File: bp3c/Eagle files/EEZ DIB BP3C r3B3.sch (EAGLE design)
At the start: 62 parts, among them IC1 TCA9534PWR, K1 RT424005, K2 RT424005, K3 RT424005, K4 RT424005, Q1 2N7002, Q2 2N7002, Q3 2N7002, Q4 2N7002, X1 ZL202-20G, X2 ZL202-20G, X3 ZL202-20G, X4 DS1023-2*14S21, X5 DS1022-2*20RF11, X6 DS1023-2*14S21, X7 N.C., X8 DS1023-2*14S21

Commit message: DIB v1.1, BP3C r3B3
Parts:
- removed X7: N.C., con-samtec:SSW-108-02-S-S
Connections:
- new net SPI4_CSC: X5-30.1
- new net SPI5_CSC: X5-34.1
- net +3V3: no longer X7-2.1, X7-3.1, X7-6.1
- net GND: no longer X5-30.1, X5-34.1, X7-1.1
- net I2C1_SCL: no longer X7-8.1
- net I2C1_SDA: no longer X7-7.1
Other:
- note added: "18 SPI3_MISO"
- note added: "20 SPI3_MOSI"
- note added: "22 SPI2_CSA"
- note added: "24 SPI2_MISO"
- note added: "26 SPI2_MOSI"
- note added: "28 SPI1_CSA"
- note added: "30 SPI2_CSC"
- note added: "32 SPI1_SCLK"
- note added: "34 SPI3_CSC"
- note added: "40-pin DIB v1.1 backplane socket"
- note added: "SPI1_CSB 27"
- note added: "SPI1_IRQ 25"
- note added: "SPI1_MISO 31"
- note added: "SPI1_MOSI 33"
- note added: "SPI2_CSB 21"
- note added: "SPI2_IRQ 19"
- note added: "SPI2_SCLK 23"
- note added: "SPI3_CSA 11"
- note added: "SPI3_CSB 13"
- note added: "SPI3_IRQ 9"
- note added: "SPI3_SCLK 17"
- note removed: "18 SPI5_MISO"
- note removed: "20 SPI5_MOSI"
- note removed: "22 SPI4_CSA"
- note removed: "24 SPI4_MISO"
- note removed: "26 SPI4_MOSI"
- note removed: "28 SPI2_CSA"
- note removed: "30 Gnd"
- note removed: "32 SPI2_SCLK"
- note removed: "34 Gnd"
- note removed: "40-pin MCU socket"
- note removed: "ADxL345 module connector (optional)"
- note removed: "SPI2_CSB 27"
- note removed: "SPI2_IRQ 25"
- note removed: "SPI2_MISO 31"
- note removed: "SPI2_MOSI 33"
- note removed: "SPI4_CSB 21"
- note removed: "SPI4_IRQ 19"
- note removed: "SPI4_SCLK 23"
- note removed: "SPI5_CSA 11"
- note removed: "SPI5_CSB 13"
- note removed: "SPI5_IRQ 9"
- note removed: "SPI5_SCLK 17"

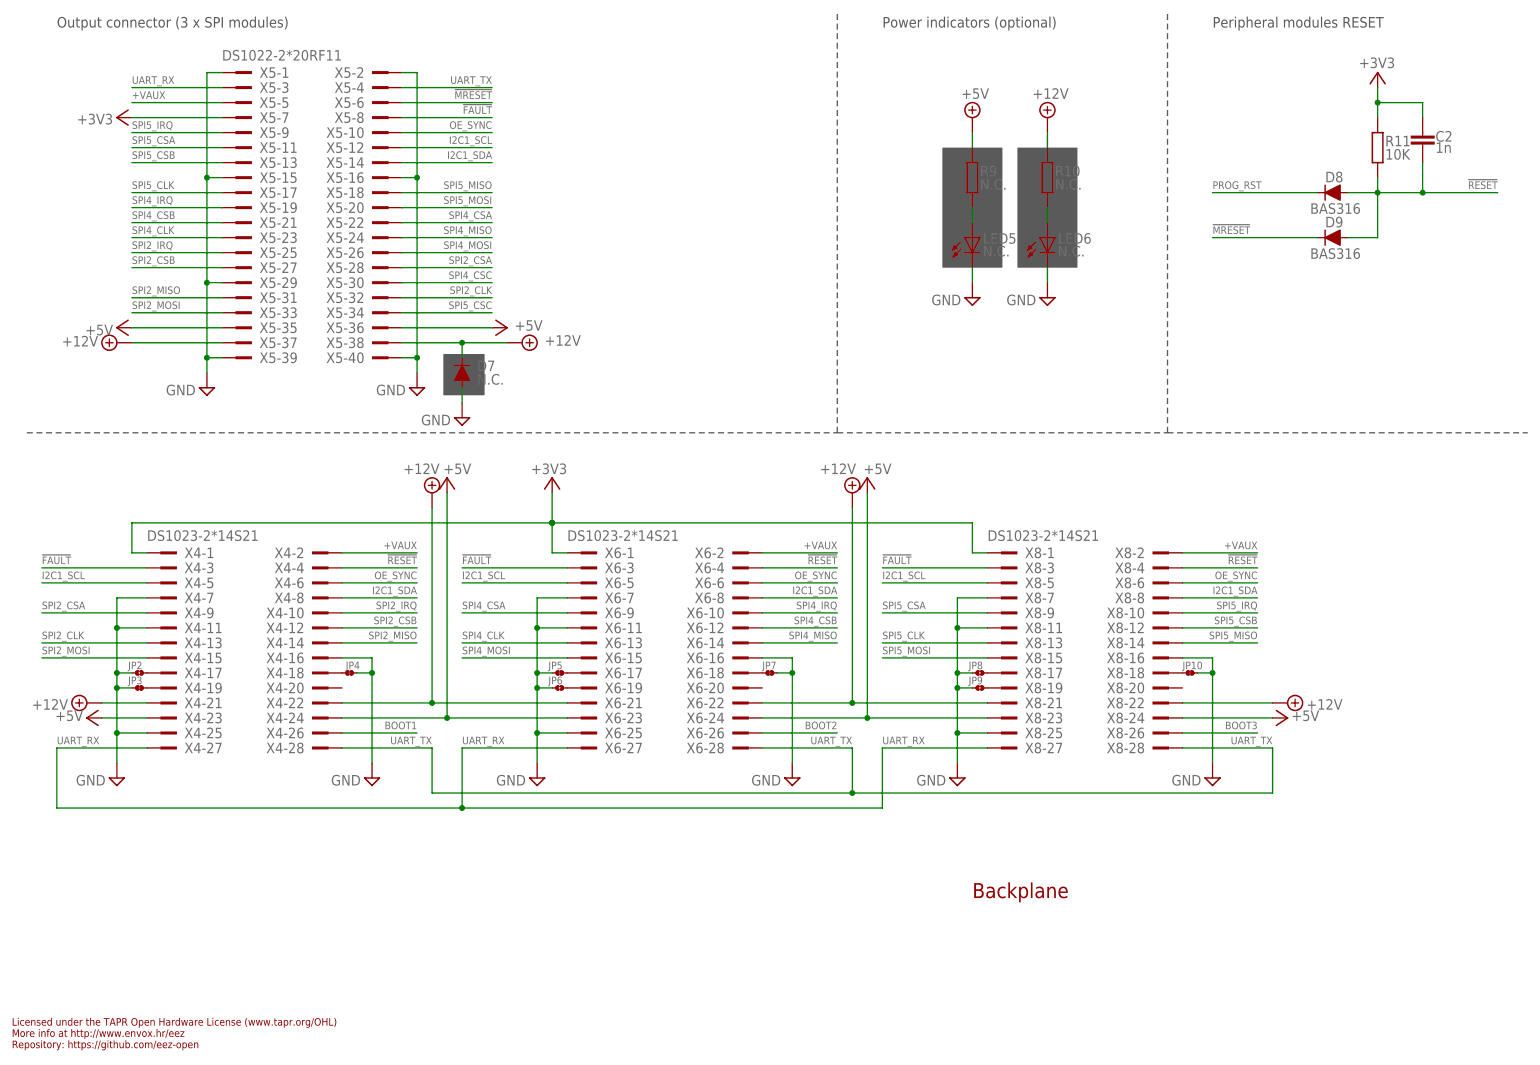
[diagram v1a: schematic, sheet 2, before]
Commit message: BP3C new ZD1-ZD4 type
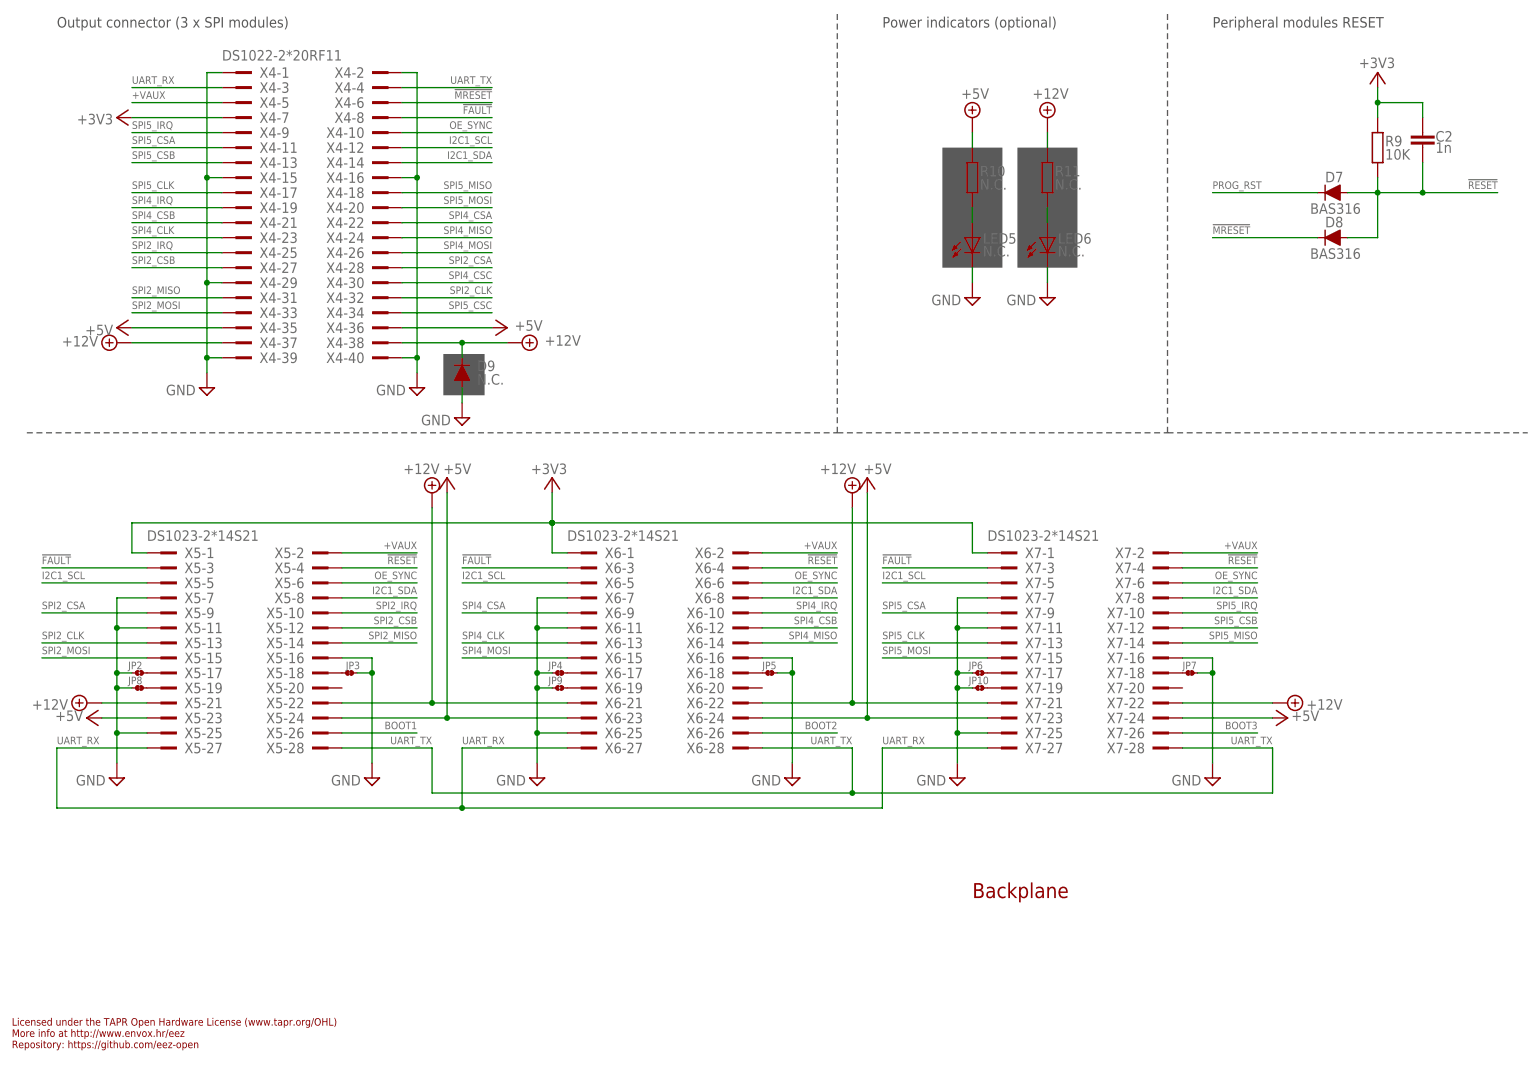
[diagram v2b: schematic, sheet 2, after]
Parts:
- D1, D2: value N.C. -> BAS316
- D3, D4: value BAS316 -> N.C.
- D7: value N.C. -> BAS316; device MyLib6:DIODEDO214AA -> EEZ_Lib1:DIODESOD323R
- D9: value BAS316 -> N.C.; device EEZ_Lib1:DIODESOD323R -> MyLib6:DIODEDO214AA
- JP10: value JP2-NOCUT -> JP2-CUT; device EEZ_Lib1:JP2-NOCUT -> EEZ_Lib1:JP2-CUT
- JP8: value JP2-CUT -> JP2-NOCUT; device EEZ_Lib1:JP2-CUT -> EEZ_Lib1:JP2-NOCUT
- R1, R5: value 100K -> N.C.
- R11: value 10K -> N.C.
- R6, R8: value N.C. -> 100K
- R9: value N.C. -> 10K
- X4: value DS1023-2*14S21 -> DS1022-2*20RF11; device EEZ_connectors:TSW-114-07-F-D -> EEZ_connectors:ZL212-40KG
- X5: value DS1022-2*20RF11 -> DS1023-2*14S21; device EEZ_connectors:ZL212-40KG -> EEZ_connectors:TSW-114-07-F-D
- ZD1, ZD2, ZD3, ZD4: value SMAJ18A -> MM3Z18VT1G; device EEZ_Lib1:PSMAXX -> EEZ_Lib1:ZENER-DIODESOD323R
- renumbered OSHWA to LABEL1, X8 to X7
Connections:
- removed net N$104 (its old number): D4.A, ZD2.A
- new net N$128: D2.A, ZD2.A
- net !FAULT: now also X4-8.1, X5-3.1; no longer X4-3.1, X5-8.1
- net !MRESET: now also D8.C, X4-6.1; no longer D9.C, X5-6.1
- net !RESET: now also D7.A, R9.2, X5-4.1; no longer D9.A, R11.2, X4-4.1
- net +12V: now also D9.C, R11.1, X4-37.1, X4-38.1, X5-21.1, X5-22.1; no longer D7.C, R10.1, X4-21.1, X4-22.1, X5-37.1, X5-38.1
- net +3V3: now also R9.1, X4-7.1, X5-1.1; no longer R11.1, X4-1.1, X5-7.1
- net +5V: now also D1.C, D2.C, R10.1, X4-35.1, X4-36.1, X5-23.1, X5-24.1; no longer D3.C, D4.C, R9.1, X4-23.1, X4-24.1, X5-35.1, X5-36.1
- net +VAUX: now also X4-5.1, X5-2.1; no longer X4-2.1, X5-5.1
- net BOOT1: now also X5-26.1; no longer X4-26.1
- net CH1_IN+: now also K4-1.P; no longer K1-1.P
- net CH1_OUT+: now also K3-1.O, K4-1.S, K4-2.O; no longer K1-1.S, K1-2.O, K2-1.O
- net CH1_OUT-: now also K1-1.O, K2-1.O, K3-2.O; no longer K2-2.O, K3-1.O, K4-1.O
- net CH2_IN+: now also K4-2.P; no longer K1-2.P
- net CH2_IN-: now also K3-2.P, K4-1.O; no longer K1-1.O, K2-2.P
- net CH2_OUT+: now also K2-1.P, K3-1.S; no longer K2-1.S, K4-1.P
- net CH2_OUT-: now also K1-1.P, K1-2.P, K3-2.S; no longer K2-2.S, K3-1.P, K3-2.P
- net CH3-: now also K1-2.O; no longer K3-2.O
- net GND: now also D9.A, JP10.1, JP3.2, JP4.1, JP5.2, R6.1, R8.1, X4-1.1, X4-15.1, X4-2.1, X4-29.1, X4-39.1, X4-40.1, X5-11.1, X5-25.1, X5-7.1; no longer D7.A, JP10.2, JP3.1, JP4.2, JP5.1, R1.1, R5.1, X4-11.1, X4-25.1, X4-7.1, X5-1.1, X5-15.1, X5-2.1, X5-29.1, X5-39.1, X5-40.1
- net I2C1_SCL: now also X4-12.1, X5-5.1; no longer X4-5.1, X5-12.1
- net I2C1_SDA: now also X4-14.1, X5-8.1; no longer X4-8.1, X5-14.1
- net N$10: now also JP4.2; no longer JP5.2
- net N$101: now also K4K.C2, Q3.D, R5.2, ZD3.C; no longer K1K.C2, Q2.D, R6.2, ZD2.C
- net N$102: now also K3K.C2, Q2.D, R3.2, ZD2.C; no longer K2K.C2, Q3.D, R7.2, ZD3.C
- net N$11: now also JP9.2; no longer JP6.2
- net N$12: now also JP7.1; no longer JP10.1
- net N$13: now also JP6.2; no longer JP8.2
- net N$14: now also JP10.2; no longer JP9.2
- net N$17: now also K1K.C2, R1.2; no longer K3K.C2, R3.2
- net N$18: now also D1.A; no longer D3.A
- net N$19: now also R1.1; no longer R3.1
- net N$2: now also JP3.1, X5-18.1; no longer JP4.1, X4-18.1
- net N$20: now also K2K.C2, R7.2; no longer K4K.C2, R8.2
- net N$22: now also R7.1; no longer R8.1
- net N$3: now also R10.2; no longer R9.2
- net N$4: now also R11.2; no longer R10.2
- net N$5: now also X5-17.1; no longer X4-17.1
- net N$6: now also JP8.2, X5-19.1; no longer JP3.2, X4-19.1
- net N$7: now also LED3.C, R5.1; no longer LED2.C, R6.1
- net N$8: now also LED2.C, R3.1; no longer LED3.C, R7.1
- net N$9: now also JP5.1; no longer JP7.1
- net OE_SYNC: now also X4-10.1, X5-6.1; no longer X4-6.1, X5-10.1
- net OUT_CGND: now also D3.C, R2.2; no longer D1.C, R1.2
- net OUT_PAR: now also D4.A, Q2.G; no longer D2.A, Q3.G
- net OUT_SER: now also D3.A, D4.C, Q3.G, R6.2; no longer D1.A, D2.C, Q2.G, R2.2
- net OUT_SRA: now also R8.2; no longer R5.2
- net PROG_RST: now also D7.C; no longer D8.C
- net SER_PAR: now also K3-1.P, K4-2.S; no longer K1-2.S, K2-1.P
- net SPI2_CLK: now also X4-32.1, X5-13.1; no longer X4-13.1, X5-32.1
- net SPI2_CSA: now also X4-28.1, X5-9.1; no longer X4-9.1, X5-28.1
- net SPI2_CSB: now also X4-27.1, X5-12.1; no longer X4-12.1, X5-27.1
- net SPI2_IRQ: now also X4-25.1, X5-10.1; no longer X4-10.1, X5-25.1
- net SPI2_MISO: now also X4-31.1, X5-14.1; no longer X4-14.1, X5-31.1
- net SPI2_MOSI: now also X4-33.1, X5-15.1; no longer X4-15.1, X5-33.1
- net SPI4_CLK: now also X4-23.1; no longer X5-23.1
- net SPI4_CSA: now also X4-22.1; no longer X5-22.1
- net SPI4_CSB: now also X4-21.1; no longer X5-21.1
- net SPI4_CSC: now also X4-30.1; no longer X5-30.1
- net SPI4_IRQ: now also X4-19.1; no longer X5-19.1
- net SPI4_MISO: now also X4-24.1; no longer X5-24.1
- net SPI4_MOSI: now also X4-26.1; no longer X5-26.1
- net SPI5_CLK: now also X4-17.1; no longer X5-17.1
- net SPI5_CSA: now also X4-11.1; no longer X5-11.1
- net SPI5_CSB: now also X4-13.1; no longer X5-13.1
- net SPI5_CSC: now also X4-34.1; no longer X5-34.1
- net SPI5_IRQ: now also X4-9.1; no longer X5-9.1
- net SPI5_MISO: now also X4-18.1; no longer X5-18.1
- net SPI5_MOSI: now also X4-20.1; no longer X5-20.1
- net UART_RX: now also X4-3.1, X5-27.1; no longer X4-27.1, X5-3.1
- net UART_TX: now also X4-4.1, X5-28.1; no longer X4-28.1, X5-4.1
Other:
- moved on the sheet: D1, D2, D3, D4, D5, D7, D8, D9, JP3, JP4, JP5, JP6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

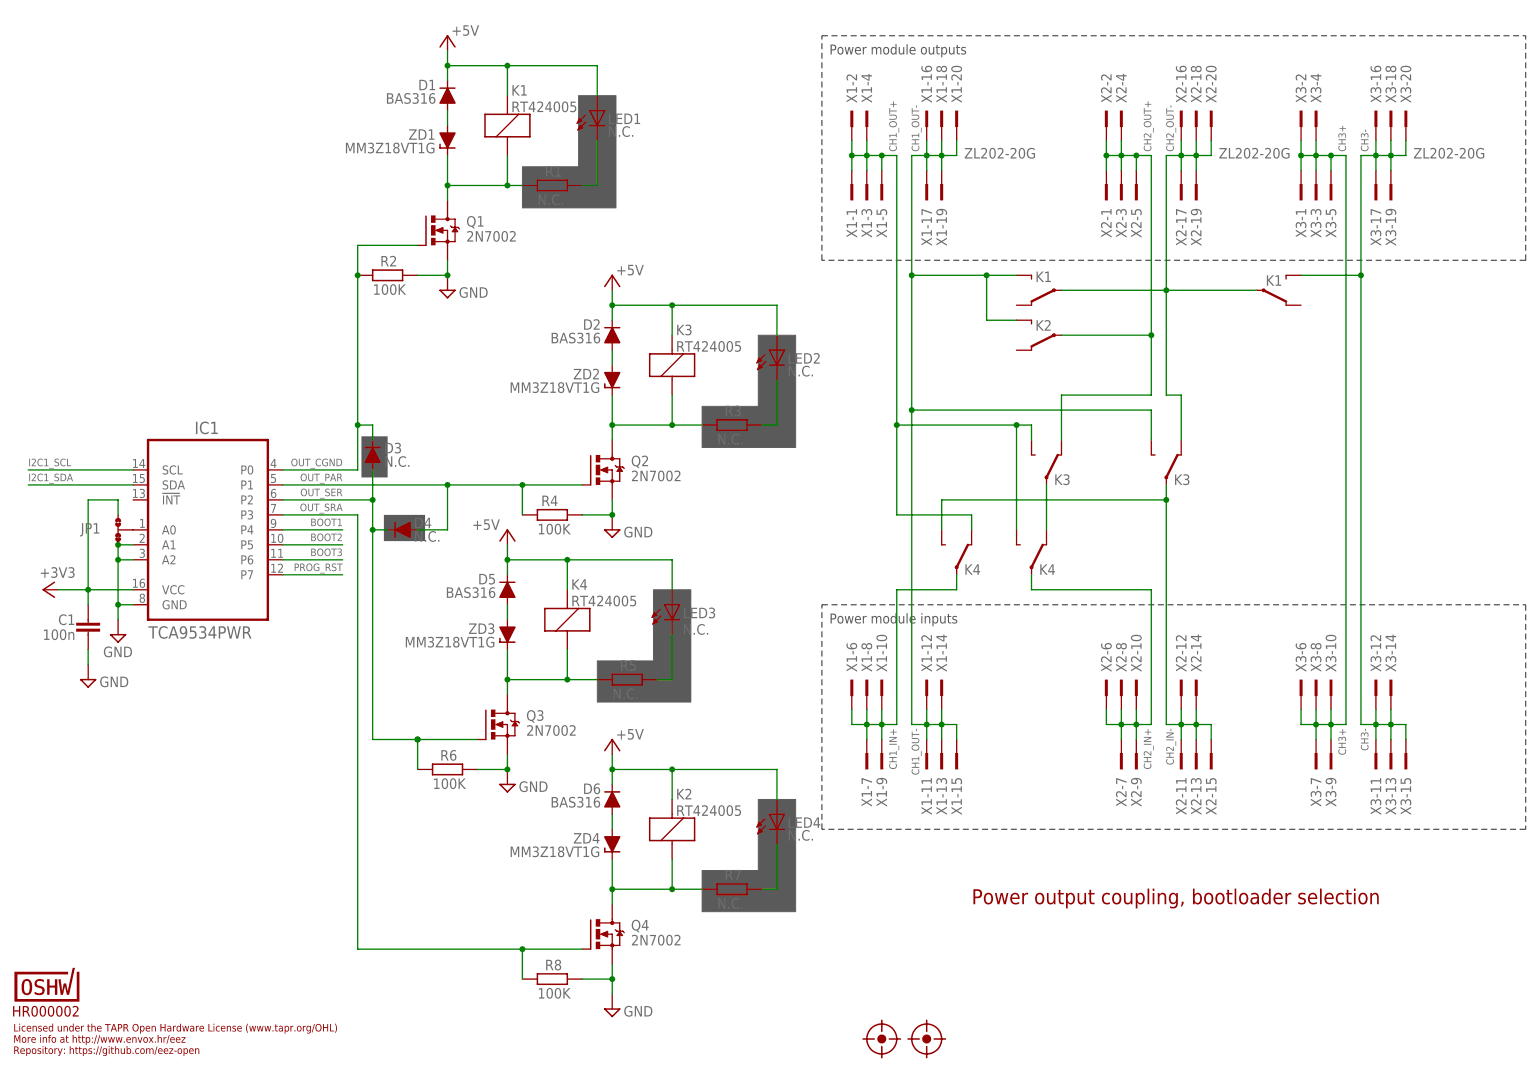
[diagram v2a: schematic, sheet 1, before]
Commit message: BP3C bottom layer cleanup
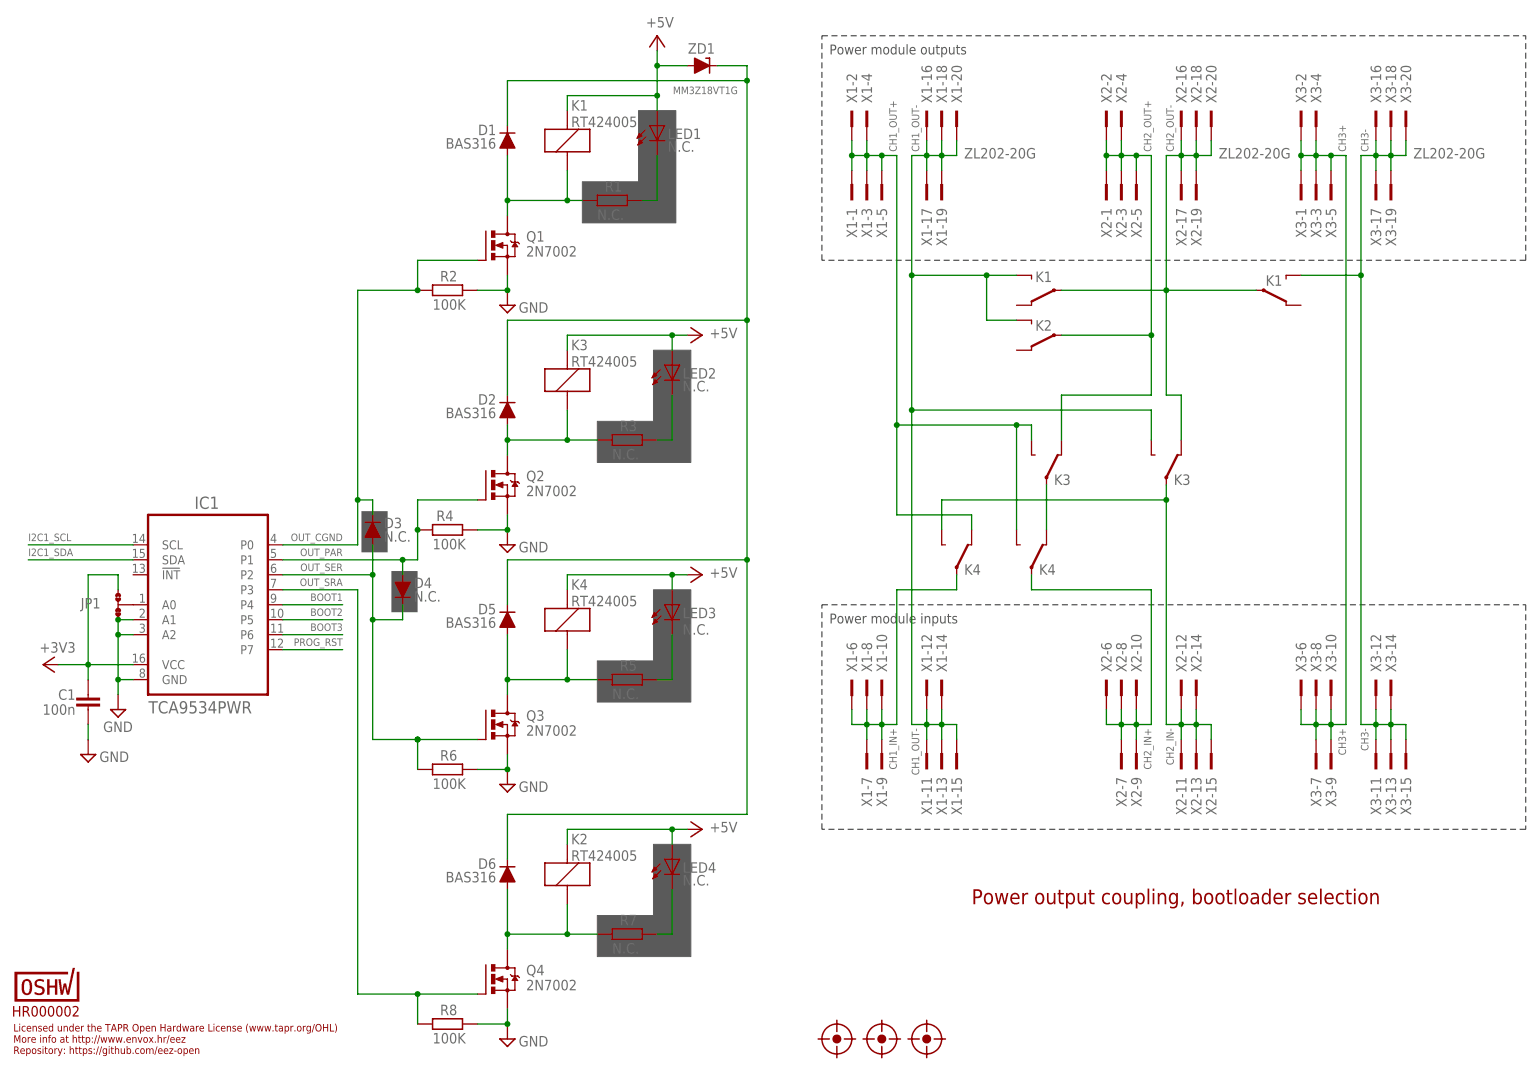
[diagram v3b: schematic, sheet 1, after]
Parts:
- removed ZD2, ZD3, ZD4: MM3Z18VT1G, EEZ_Lib1:ZENER-DIODESOD323R
- added FM3: FIDUCIAL, EEZ_Lib1:FIDUCIAL
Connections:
- removed net N$104: D5.A, ZD3.A
- removed net N$128: D2.A, ZD2.A
- removed net N$18: D1.A, ZD1.A
- removed net N$21: D6.A, ZD4.A
- new net N$16: D1.C, D2.C, D5.C, D6.C, ZD1.C
- net +5V: now also ZD1.A; no longer D1.C, D2.C, D5.C, D6.C
- net N$101: now also D5.A; no longer ZD3.C
- net N$102: now also D2.A; no longer ZD2.C
- net N$17: now also D1.A; no longer ZD1.C
- net N$20: now also D6.A; no longer ZD4.C
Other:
- moved on the sheet: C1, D1, D2, D3, D4, D5, D6, IC1, JP1, K1, K2, K3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
